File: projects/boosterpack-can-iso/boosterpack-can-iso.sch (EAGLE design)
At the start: 2 parts

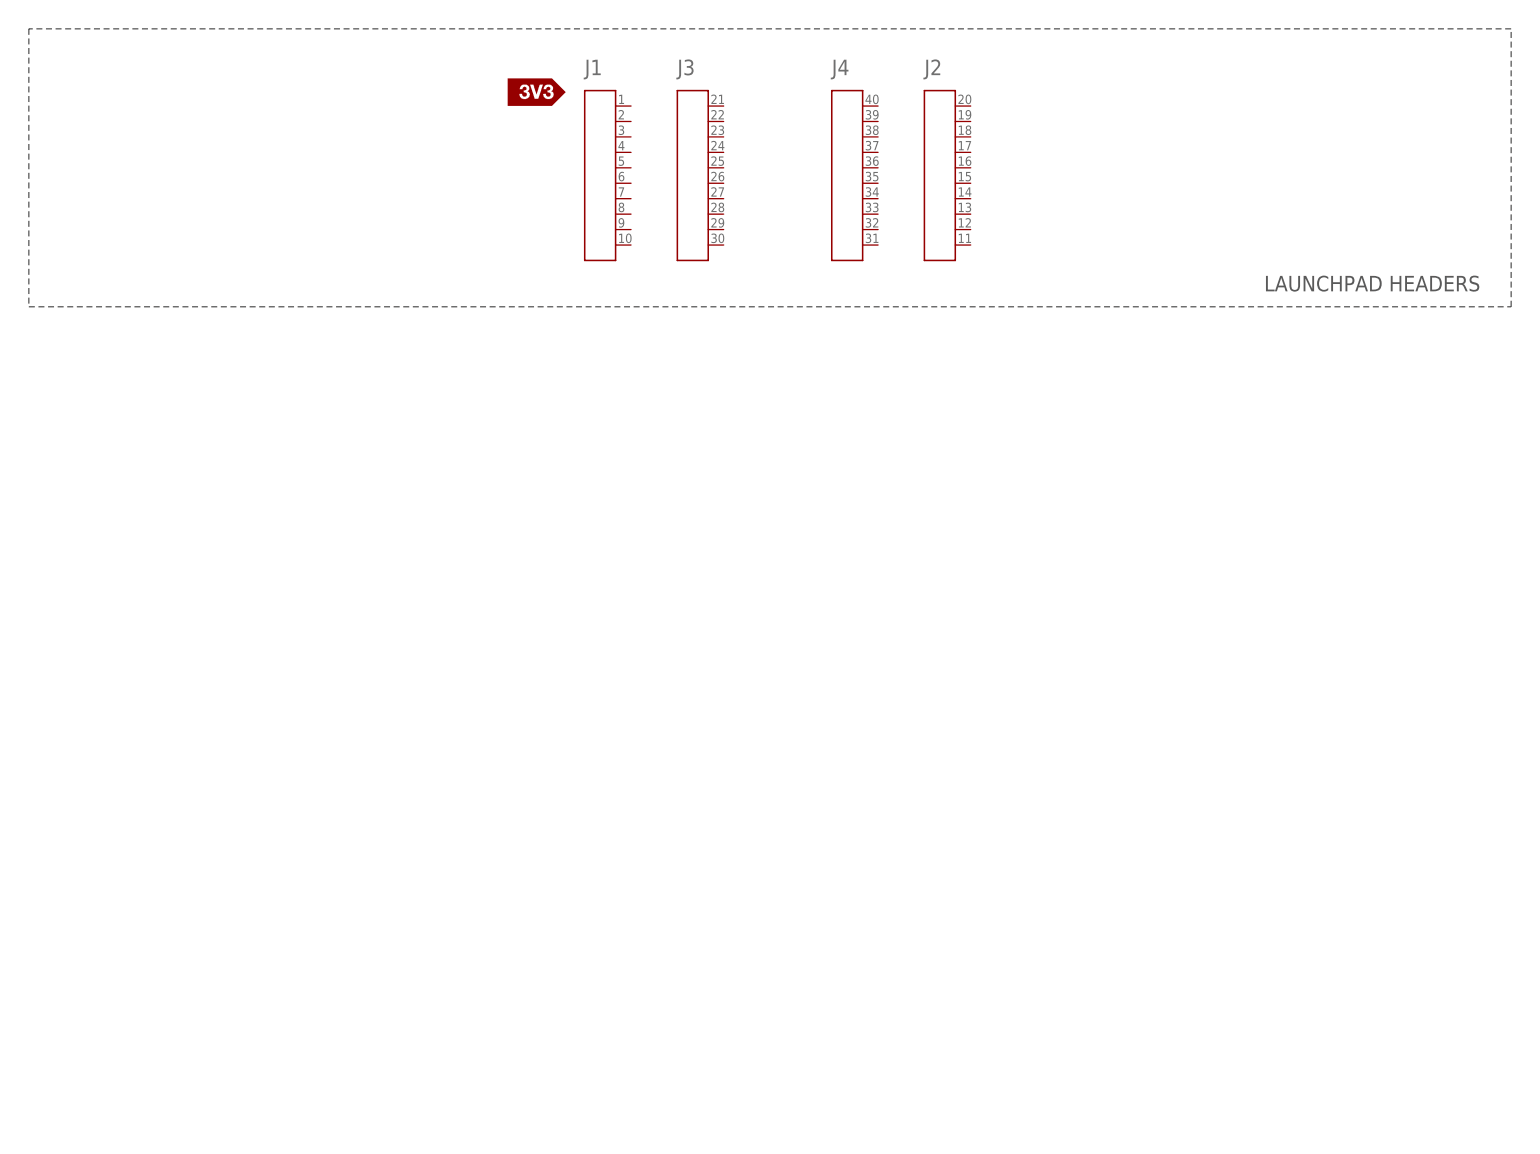
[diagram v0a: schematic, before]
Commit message: Added markdown documentation files.
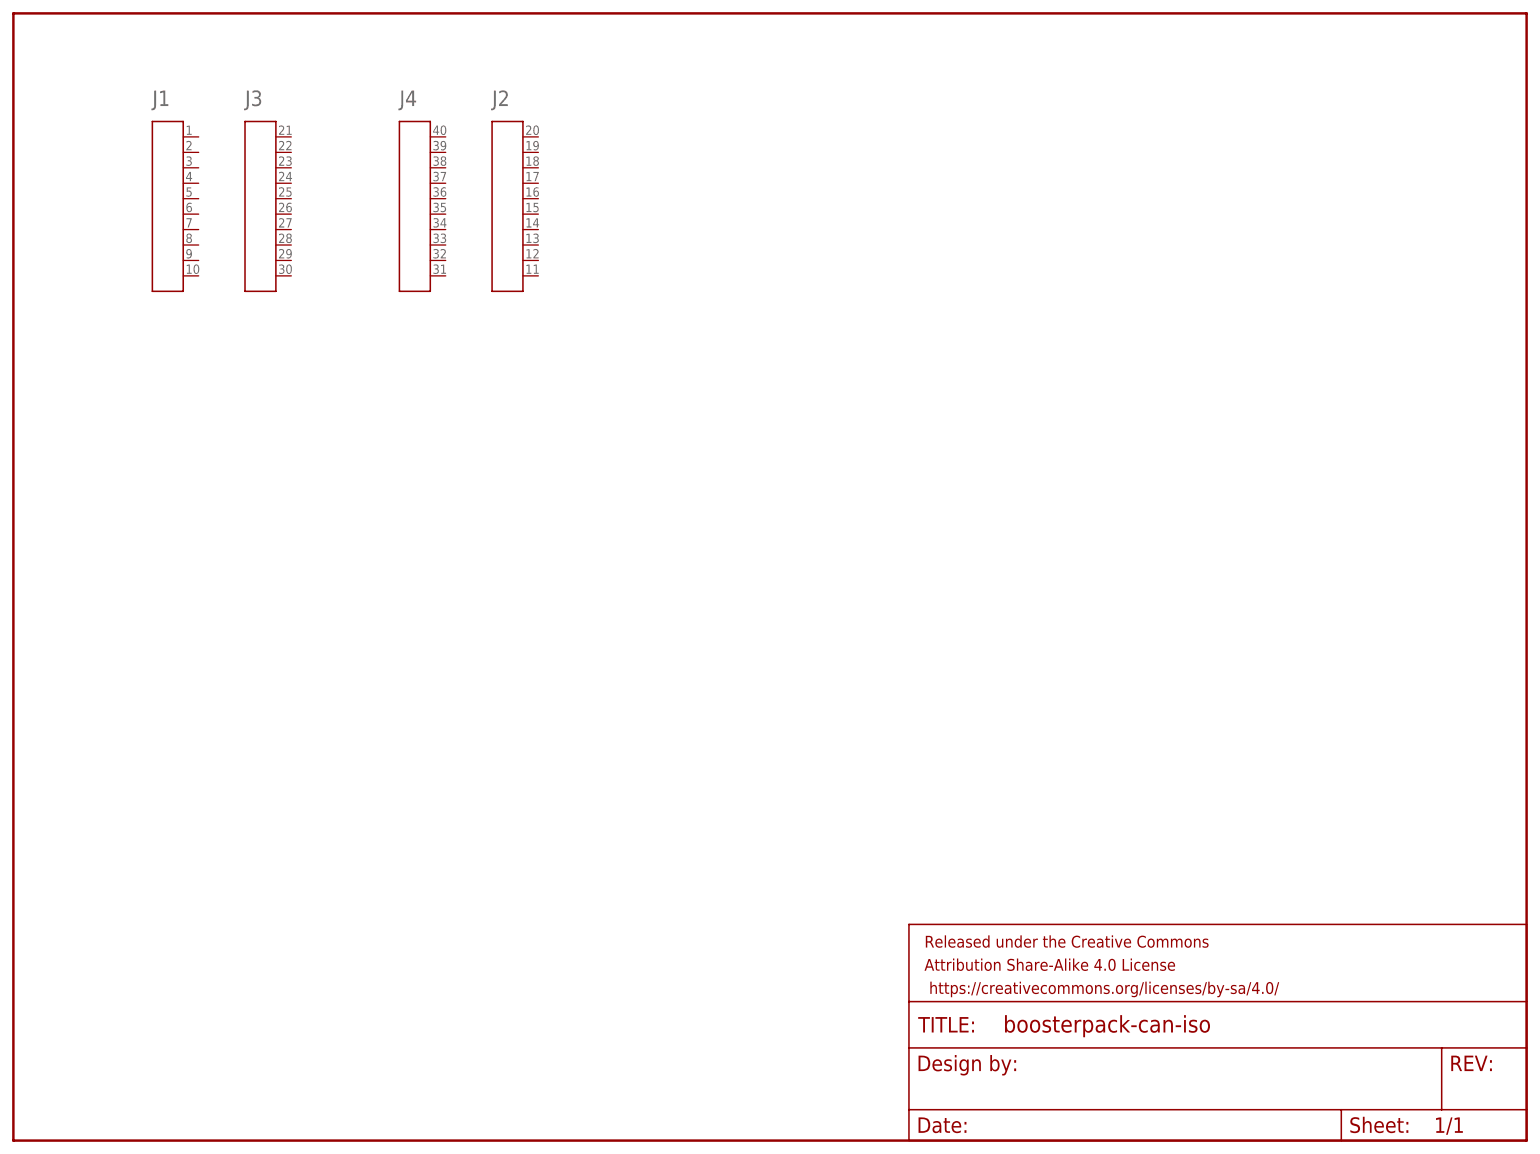
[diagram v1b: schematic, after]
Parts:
- removed U$3: SILK_3V3_TAG, Public_BP_Library:SILK_3V3_TAG
- added FRAME1: FRAME-LETTERNO_PACKAGE, SparkFun-Aesthetics:FRAME-LETTERNO_PACKAGE
- added U$1: LOGO-ROCKET, EAGLE_BoosterPack_Library:LOGO-ROCKET
- A1: device Public_BP_Library:HEADER4X10-BOOSTERPACK -> EAGLE_BoosterPack_Library:HEADER4X10-BOOSTERPACK
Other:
- note removed: "LAUNCHPAD HEADERS"
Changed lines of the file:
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@@
 <layers>
 <layer number="1" name="Top" color="4" fill="1" visible="no" active="no"/>
-<layer number="2" name="Route2" color="1" fill="3" visible="no" active="no"/>
-<layer number="3" name="Route3" color="4" fill="3" visible="no" active="no"/>
-<layer number="14" name="Route14" color="1" fill="6" visible="no" active="no"/>
-<layer number="15" name="Route15" color="4" fill="6" visible="no" active="no"/>
 <layer number="16" name="Bottom" color="1" fill="1" visible="no" active="no"/>
 <layer number="17" name="Pads" color="2" fill="1" visible="no" active="no"/>
@@
 <layer number="19" name="Unrouted" color="6" fill="1" visible="no" active="no"/>
 <layer number="20" name="Dimension" color="15" fill="1" visible="no" active="no"/>
-<layer number="21" name="tPlace" color="16" fill="1" visible="no" active="no"/>
-<layer number="22" name="bPlace" color="14" fill="1" visible="no" active="no"/>
+<layer number="21" name="tPlace" color="7" fill="1" visible="no" active="no"/>
+<layer number="22" name="bPlace" color="7" fill="1" visible="no" active="no"/>
 <layer number="23" name="tOrigins" color="15" fill="1" visible="no" active="no"/>
 <layer number="24" name="bOrigins" color="15" fill="1" visible="no" active="no"/>
@@
 <layer number="27" name="tValues" color="7" fill="1" visible="no" active="no"/>
 <layer number="28" name="bValues" color="7" fill="1" visible="no" active="no"/>
-<layer number="29" name="tStop" color="7" fill="3" visible="no" active="no"/>
+<layer number="29" name="tStop" color="15" fill="3" visible="no" active="no"/>
 <layer number="30" name="bStop" color="7" fill="6" visible="no" active="no"/>
 <layer number="31" name="tCream" color="7" fill="4" visible="no" active="no"/>
@@
 <layer number="47" name="Measures" color="7" fill="1" visible="no" active="no"/>
 <layer number="48" name="Document" color="7" fill="1" visible="no" active="no"/>
-<layer number="49" name="Reference" color="7" fill="1" visible="no" active="no"/>
+<layer number="49" name="Reference" color="13" fill="1" visible="no" active="no"/>
 <layer number="50" name="dxf" color="7" fill="1" visible="no" active="no"/>
-<layer number="51" name="tDocu" color="6" fill="1" visible="no" active="no"/>
+<layer number="51" name="tDocu" color="14" fill="1" visible="no" active="no"/>
 <layer number="52" name="bDocu" color="7" fill="1" visible="no" active="no"/>
 <layer number="53" name="tGND_GNDA" color="7" fill="9" visible="no" active="no"/>
@@
 <layer number="59" name="tCarbon" color="7" fill="1" visible="no" active="no"/>
 <layer number="60" name="bCarbon" color="7" fill="1" visible="no" active="no"/>
+<layer number="90" name="Modules" color="5" fill="1" visible="yes" active="yes"/>
 <layer number="91" name="Nets" color="2" fill="1" visible="yes" active="yes"/>
 <layer number="92" name="Busses" color="1" fill="1" visible="yes" active="yes"/>
@@
 <layer number="97" name="Info" color="7" fill="1" visible="yes" active="yes"/>
 <layer number="98" name="Guide" color="6" fill="1" visible="yes" active="yes"/>
-<layer number="99" name="SpiceOrder" color="5" fill="1" visible="yes" active="yes"/>
+<layer number="99" name="SpiceOrder" color="7" fill="1" visible="no" active="no"/>
 <layer number="100" name="Muster" color="7" fill="1" visible="no" active="no"/>
 <layer number="101" name="Patch_Top" color="12" fill="4" visible="yes" active="yes"/>
@@
 <layer number="106" name="bPlate" color="7" fill="1" visible="yes" active="yes"/>
 <layer number="107" name="Crop" color="7" fill="1" visible="yes" active="yes"/>
-<layer number="108" name="fp8" color="7" fill="1" visible="yes" active="yes"/>
-<layer number="109" name="fp9" color="7" fill="1" visible="yes" active="yes"/>
+<layer number="108" name="tplace-old" color="10" fill="1" visible="yes" active="yes"/>
+<layer number="109" name="ref-old" color="11" fill="1" visible="yes" active="yes"/>
 <layer number="110" name="fp0" color="7" fill="1" visible="yes" active="yes"/>
 <layer number="111" name="LPC17xx" color="7" fill="1" visible="yes" active="yes"/>
 <layer number="112" name="tSilk" color="7" fill="1" visible="yes" active="yes"/>
+<layer number="113" name="IDFDebug" color="4" fill="1" visible="yes" active="yes"/>
 <layer number="116" name="Patch_BOT" color="9" fill="4" visible="yes" active="yes"/>
 <layer number="118" name="Rect_Pads" color="7" fill="1" visible="no" active="no"/>
@@
 <layer number="127" name="_tValues" color="7" fill="1" visible="yes" active="yes"/>
 <layer number="128" name="_bValues" color="7" fill="1" visible="yes" active="yes"/>
-<layer number="129" name="Mask" color="7" fill="1" visible="no" active="yes"/>
+<layer number="129" name="Mask" color="7" fill="1" visible="yes" active="yes"/>
 <layer number="130" name="130bmp" color="2" fill="1" visible="no" active="yes"/>
 <layer number="131" name="tAdjust" color="7" fill="1" visible="yes" active="yes"/>
@@
 <layer number="151" name="HeatSink" color="7" fill="1" visible="yes" active="yes"/>
 <layer number="152" name="_bDocu" color="7" fill="1" visible="yes" active="yes"/>
-<layer number="153" name="FabDoc1" color="6" fill="1" visible="no" active="no"/>
-<layer number="154" name="FabDoc2" color="2" fill="1" visible="no" active="no"/>
-<layer number="155" name="FabDoc3" color="7" fill="15" visible="no" active="no"/>
-<layer number="199" name="Contour" color="7" fill="1" visible="no" active="yes"/>
+<layer number="153" name="FabDoc1" color="7" fill="1" visible="yes" active="yes"/>
+<layer number="154" name="FabDoc2" color="7" fill="1" visible="yes" active="yes"/>
+<layer number="155" name="FabDoc3" color="7" fill="1" visible="yes" active="yes"/>
+<layer number="199" name="Contour" color="7" fill="1" visible="yes" active="yes"/>
 <layer number="200" name="200bmp" color="1" fill="10" visible="yes" active="yes"/>
 <layer number="201" name="201bmp" color="2" fill="10" visible="yes" active="yes"/>
@@
 <layer number="223" name="223bmp" color="24" fill="1" visible="no" active="no"/>
 <layer number="224" name="224bmp" color="25" fill="1" visible="no" active="no"/>
-<layer number="231" name="Eagle3D_PG1" color="14" fill="1" visible="no" active="yes"/>
+<layer number="225" name="225bmp" color="7" fill="1" visible="yes" active="yes"/>
+<layer number="226" name="226bmp" color="7" fill="1" visible="yes" active="yes"/>
+<layer number="227" name="227bmp" color="7" fill="1" visible="yes" active="yes"/>
+<layer number="228" name="228bmp" color="7" fill="1" visible="yes" active="yes"/>
+<layer number="229" name="229bmp" color="7" fill="1" visible="yes" active="yes"/>
+<layer number="230" name="230bmp" color="7" fill="1" visible="yes" active="yes"/>
+<layer number="231" name="231bmp" color="7" fill="1" visible="yes" active="yes"/>
 <layer number="232" name="Eagle3D_PG2" color="14" fill="2" visible="no" active="yes"/>
 <layer number="233" name="Eagle3D_PG3" color="14" fill="4" visible="no" active="yes"/>
@@
 <layer number="251" name="SMDround" color="12" fill="11" visible="no" active="no"/>
 <layer number="254" name="cooling" color="7" fill="1" visible="yes" active="yes"/>
+<layer number="255" name="routoute" color="7" fill="1" visible="yes" active="yes"/>
 </layers>
 <schematic xreflabel="%F%N/%S.%C%R" xrefpart="/%S.%C%R">
@@
 </classes>
 <parts>
-<part name="FRAME1" library="frames" deviceset="LETTER_L" device=""/>
-<part name="A1" library="Public_BP_Library" deviceset="HEADER4X10-BOOSTERPACK" device=""/>
-<part name="U$3" library="Public_BP_Library" deviceset="SILK_3V3_TAG" device=""/>
+<part name="FRAME1" library="SparkFun-Aesthetics" deviceset="FRAME-LETTER" device="NO_PACKAGE"/>
+<part name="A1" library="EAGLE_BoosterPack_Library" deviceset="HEADER4X10-BOOSTERPACK" device=""/>
+<part name="U$1" library="EAGLE_BoosterPack_Library" deviceset="LOGO-ROCKET" device=""/>
 </parts>
 <sheets>
 <sheet>
 <plain>
-<text x="205.74" y="139.7" size="2.54" layer="97" ratio="12">LAUNCHPAD HEADERS</text>
-<wire x1="2.54" y1="182.88" x2="2.54" y2="137.16" width="0.2032" layer="97" style="longdash"/>
-<wire x1="2.54" y1="137.16" x2="246.38" y2="137.16" width="0.2032" layer="97" style="longdash"/>
-<wire x1="246.38" y1="137.16" x2="246.38" y2="182.88" width="0.2032" layer="97" style="longdash"/>
-<wire x1="246.38" y1="182.88" x2="2.54" y2="182.88" width="0.2032" layer="97" style="longdash"/>
 </plain>
 <instances>
-<instance part="FRAME1" gate="G$1" x="0" y="0" smashed="yes"/>
-<instance part="FRAME1" gate="G$2" x="147.32" y="0"/>
-<instance part="A1" gate="G$1" x="96.52" y="157.48"/>
-<instance part="U$3" gate="G$1" x="81.28" y="170.18"/>
+<instance part="FRAME1" gate="G$1" x="0" y="0"/>
+<instance part="FRAME1" gate="V" x="147.32" y="0"/>
+<instance part="A1" gate="G$1" x="25.4" y="152.4"/>
 </instances>
 <busses>
@@
 </sheet>
 </sheets>
-<errors>
-</errors>
 </schematic>
 </drawing>
